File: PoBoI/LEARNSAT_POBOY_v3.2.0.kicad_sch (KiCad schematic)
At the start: 0 parts

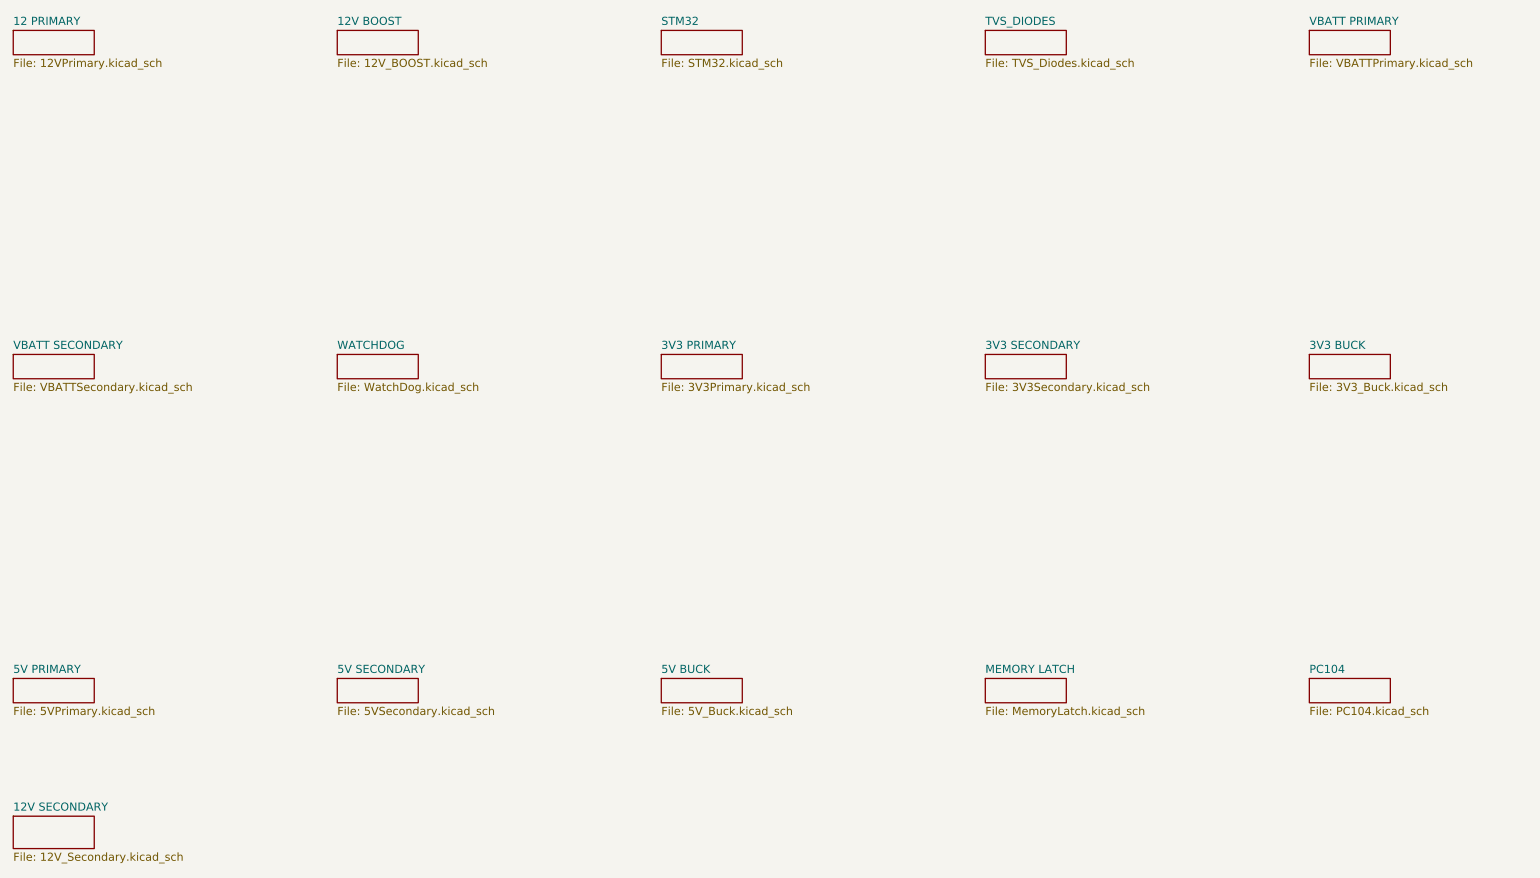
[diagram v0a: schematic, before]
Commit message: POBOI 4S updates: remove 12V/TVS sheets, fix VBATT dividers, INA219 addresses, U26
POBOI changes 10/28 Simon Ionashku

- Deleted the separate copy of the PCB file (BoardFix, it was an older version)
- Removed these sheets from the schematic and the board (no use for them anymore)
   - 12 PRIMARY
   - 12V BOOST
   - 12V SECONDARY
      - our 4S pack is already 12-16.8V so boosting to 12V does nothing, and the LM2622 is only rated for 12V in anyway
      - anything that needs ~12V can just use the VBATT Primary/Secondary rails
      - also deleted the "NEED TO ADD 12V COMPATIBILITY" note on the STM32 sheet
   - TVS_DIODES
      - they weren't actually connected to anything (cathodes were all no-connects)
      - they're also just 3.6V zeners, not real TVS diodes
      - the LTC4231 already shuts off on overvoltage, undervoltage and overcurrent, and there's a small zener clamp on each enable line
- Fixed the VBATT Primary and Secondary divider resistors since they were still using the 2S numbers and we moved to 4S
   - with the old values the switches would've never turned on (they cut off above ~8V)
   - new thresholds: OVoff = 17.5V, UVon = 12.4V, UVoff = 12.0V (3.0V per cell)
   - RES    OLD     NEW
      R71    866k    931k   (Primary)
      R74    2.37k   2.15k  (Primary)
      R77    37.4k   18.7k  (Primary)
      R78    100k    45.3k  (Primary)
      R68    866k    931k   (Secondary)
      R65    2.37k   2.15k  (Secondary)
      R63    37.4k   18.7k  (Secondary)
      R64    100k    45.3k  (Secondary)
   - updated the values, part numbers and form factor (all 0603 now) in the BOM and field table
      - R68/R71 were 0201 rated for 25V which is cutting it close at 16.8V
   - updated the notes and calculations on both sheets
- Fixed the INA219 addresses
   - a bunch of the A0/A1 pins were floating (marked no-connect) so the addresses would've been random
   - went through and checked/corrected all six so A0 and A1 match the slave address table
      5V Primary    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
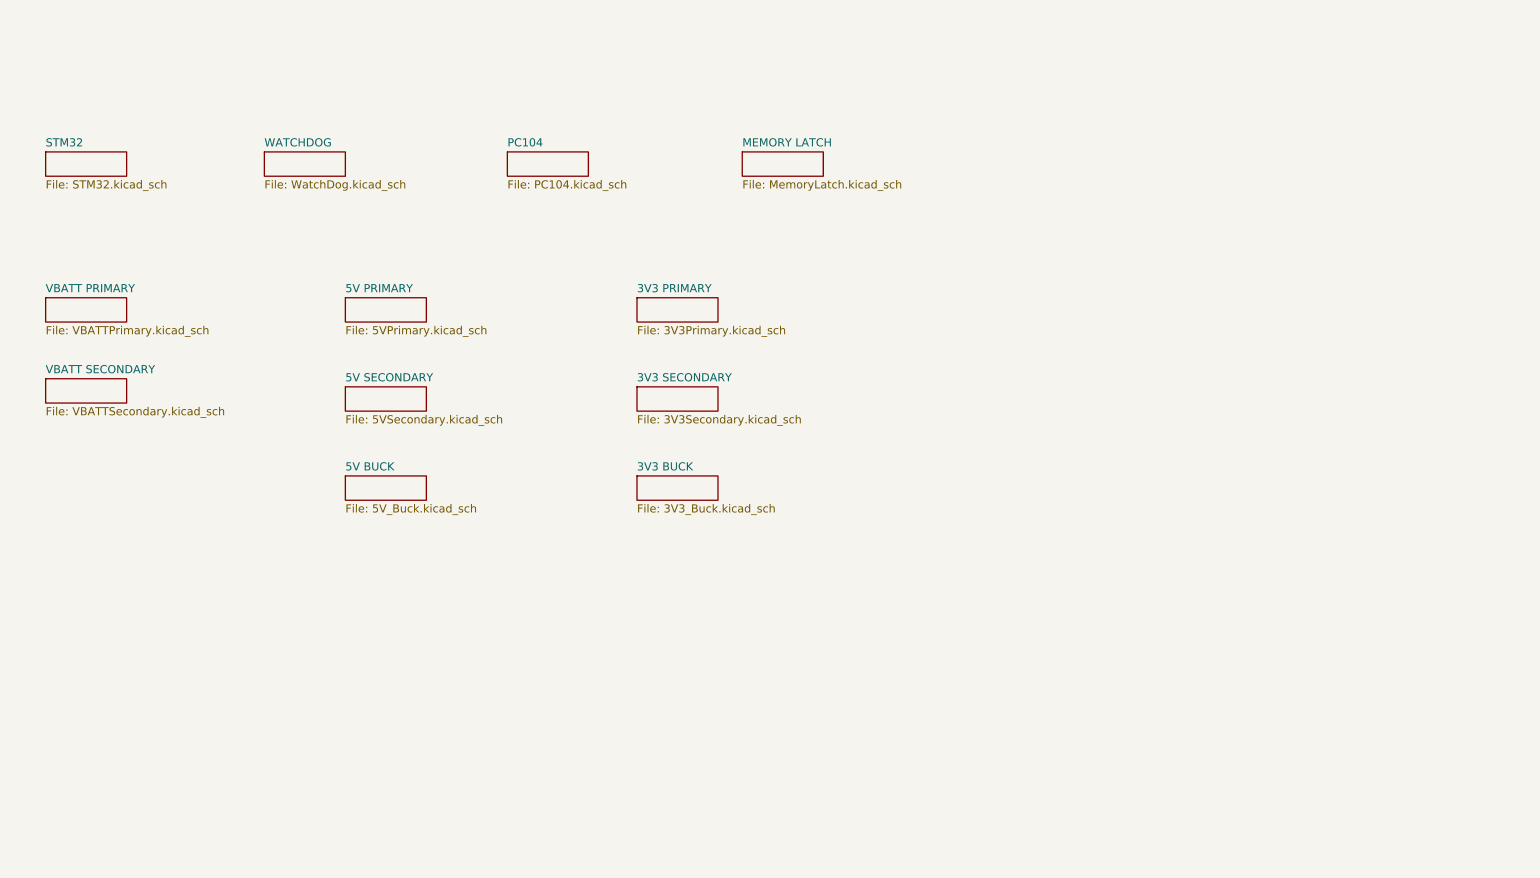
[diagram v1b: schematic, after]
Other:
- removed sheet 12 PRIMARY
- removed sheet 12V BOOST
- removed sheet 12V SECONDARY
- removed sheet TVS_DIODES
